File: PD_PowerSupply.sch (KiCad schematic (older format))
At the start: 79 parts, among them J1 Connector, J2 Connector, J3 Connector, J4 Connector, Q1 STL6P3LLH6, Q2 STL6P3LLH6, Q3 MMBT3906, Q4 MMBT3906, U1 nRF52840, U2 STUSB4500QTR, U3 STM32L432KCUx, U4 LTM8074IY#PBF, U5 LTC2972, U6 LTM8074IY#PBF, U7 LTM8074IY#PBF

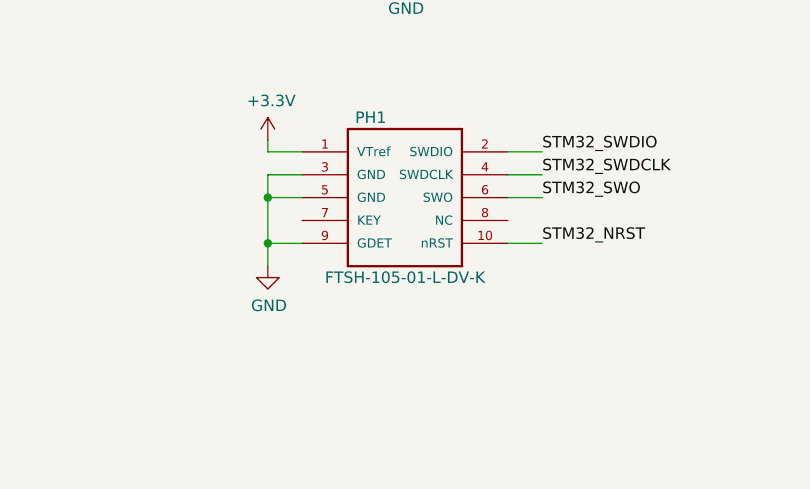
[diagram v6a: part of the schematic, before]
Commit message: added secondary 2.54 headers
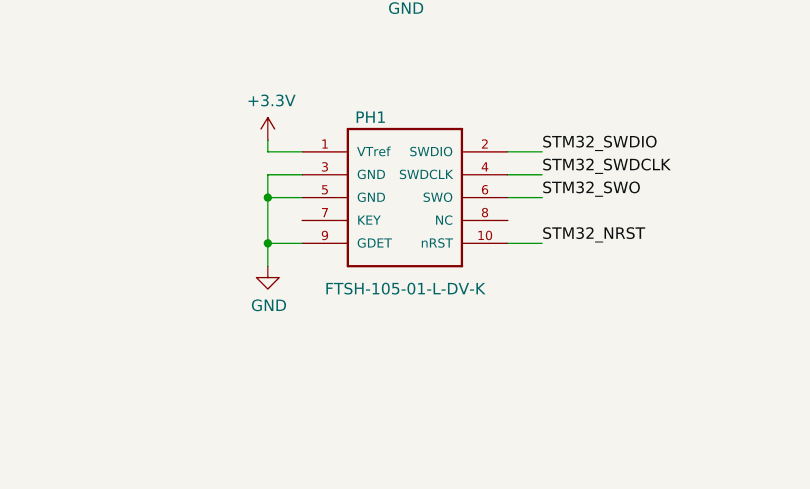
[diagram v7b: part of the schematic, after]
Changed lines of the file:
@@
 P 8700 14600
 F 0 "PH1" H 8600 14950 50  0000 C CNN
-F 1 "FTSH-105-01-L-DV-K" H 8750 14250 50  0000 C CNN
+F 1 "FTSH-105-01-L-DV-K" H 8750 14200 50  0000 C CNN
 F 2 "SAMTEC_FTSH-105-01-L-DV-K" H 8700 14600 50  0001 L BNN
 F 3 "G" H 8700 14600 50  0001 L BNN

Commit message: started routing switchers
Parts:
- added +3V3, GND1, I2C_SCL1, I2C_SDA1, P0.13, P0.14, P0.15, P0.16, P0.17, P0.19, P0.20, P0.21, PMB_SCL1, PMB_SDA1: TestPoint, TestPoint:TestPoint_Pad_D1.0mm, symbol Connector:TestPoint
- added C19, C20: 10uF, Capacitor_SMD:C_0805_2012Metric, symbol Device:C
- added D4: BLUE 0805, LED_SMD:LED_0805_2012Metric, symbol Device:LED
- added D5: ORANGE 0805, LED_SMD:LED_0805_2012Metric, symbol Device:LED
- added JP3: SolderJumper_2_Bridged, Jumper:SolderJumper-2_P1.3mm_Bridged_RoundedPad1.0x1.5mm, symbol Jumper:SolderJumper_2_Bridged
- added R35, R36: 300, Resistor_SMD:R_0603_1608Metric, symbol Device:R_US
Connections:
- net +3V3: now also +3V3.1, R36.1
- net GND: now also C19.1, C20.1, GND1.1, R35.1
- net I2C_SCL: now also I2C_SCL1.1
- net I2C_SCL_SMBUS: now also PMB_SCL1.1
- net I2C_SDA: now also I2C_SDA1.1
- net I2C_SDA_SMBUS: now also PMB_SDA1.1
- net SPI_MISO: now also P0.14.1
- net SPI_MOSI: now also P0.15.1
- net SPI_SCK: now also P0.13.1
- net SPI_SS: now also P0.16.1
- net UART_RX: now also P0.17.1
- net UART_TX: now also P0.19.1
- net at U2.14 (POWER_OK3): now also D5.1 (K), JP3.2 (B)
- net at U2.20 (POWER_OK2): now also JP3.1 (A)
- net at R28.1, U5.34 (ISENSEP1), U6.E1 (VOUT)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: now also C20.2
- net at R18.1, U4.E1 (VOUT), U4.E2 (VOUT)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: now also C19.2
- net at U1.AC17 (P0.21): now also P0.21.1
- net at U1.AD16 (P0.20): now also P0.20.1
- net at U1.U1 (TRACEDATA1/P0.12): now also D4.2 (A)
- new net: D4.1 (K), R35.2
- new net: D5.2 (A), R36.2
- no-connect marks 7 -> 5
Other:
- note added: "0805\n"
- moved on the sheet: R1, R4
